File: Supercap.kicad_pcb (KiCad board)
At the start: 4 copper layers, 139 x 70.9 mm, 81 parts, among them IC1 NCP5109ADR2G, IC2 NCP5109ADR2G, J1 Conn_01x01, J2 Conn_01x01, J2-J1 Conn_01x10, J3 XT30, J3-J1 Conn_01x10, J4 XT30, P7803B-1000R1 P7803B-1000, P7812B-1000R1 490-P7812B-1000, U1 TLV2372, U2 TLV2372, U3 ACS71240KEXBLT-010B3, U4 LP-MSPM0G3507

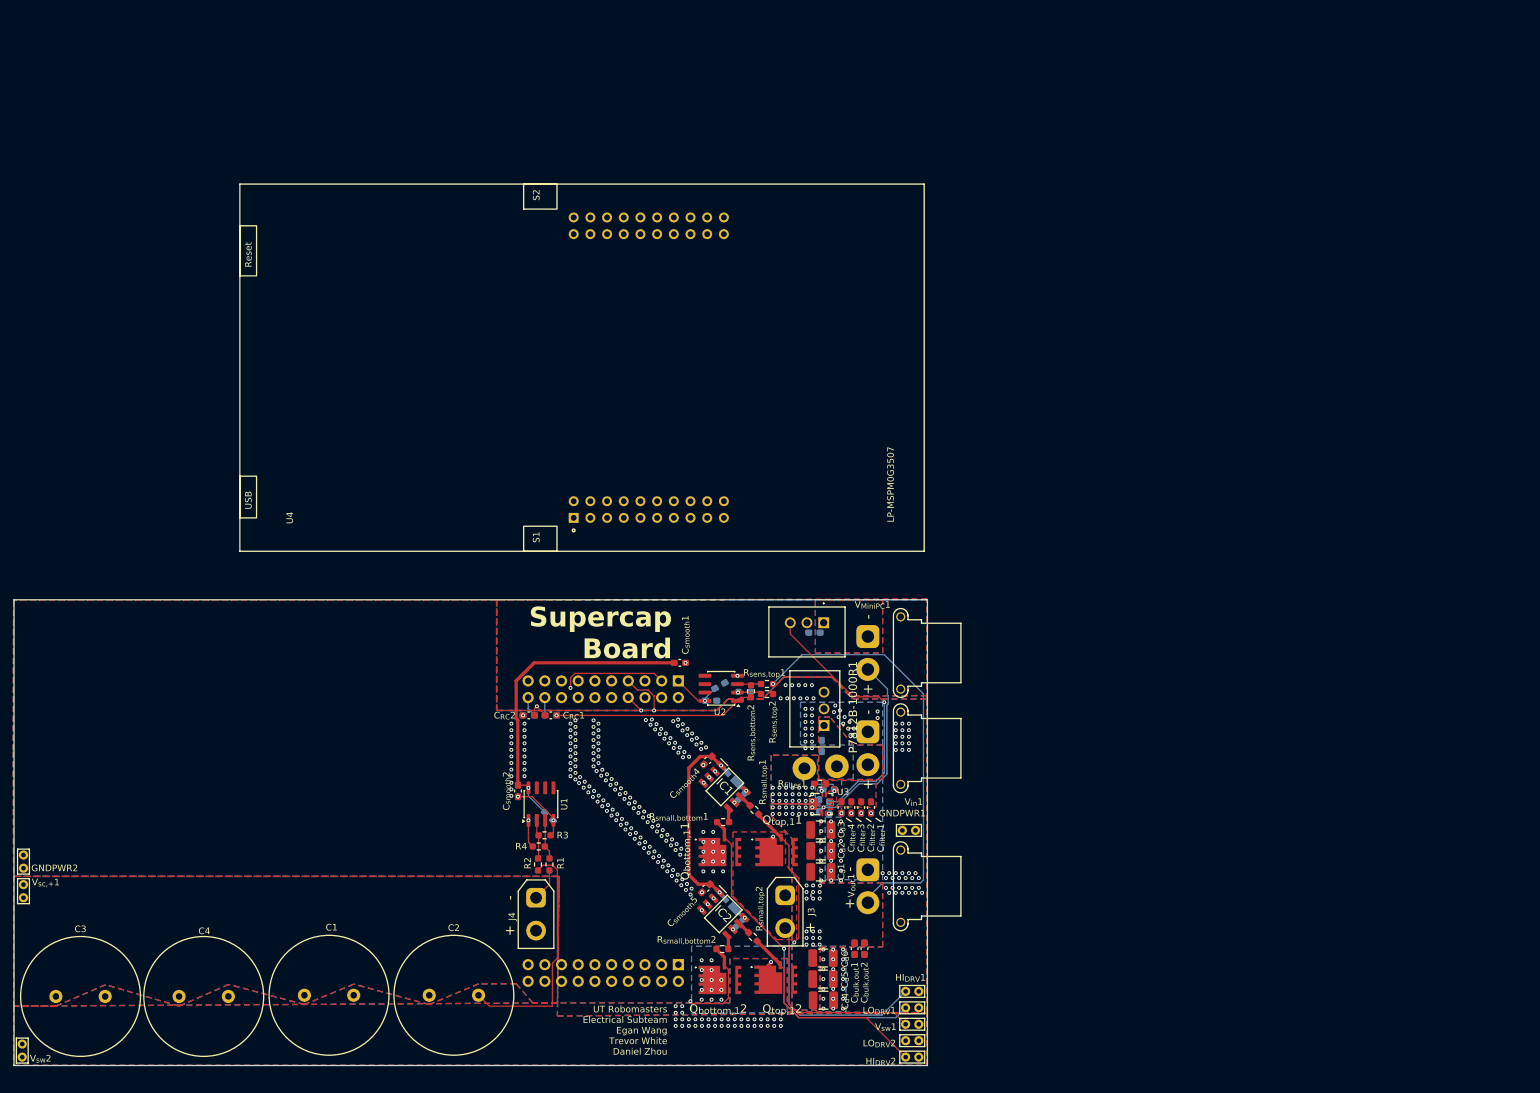
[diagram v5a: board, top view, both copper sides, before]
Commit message: split into separate boards as per regulations
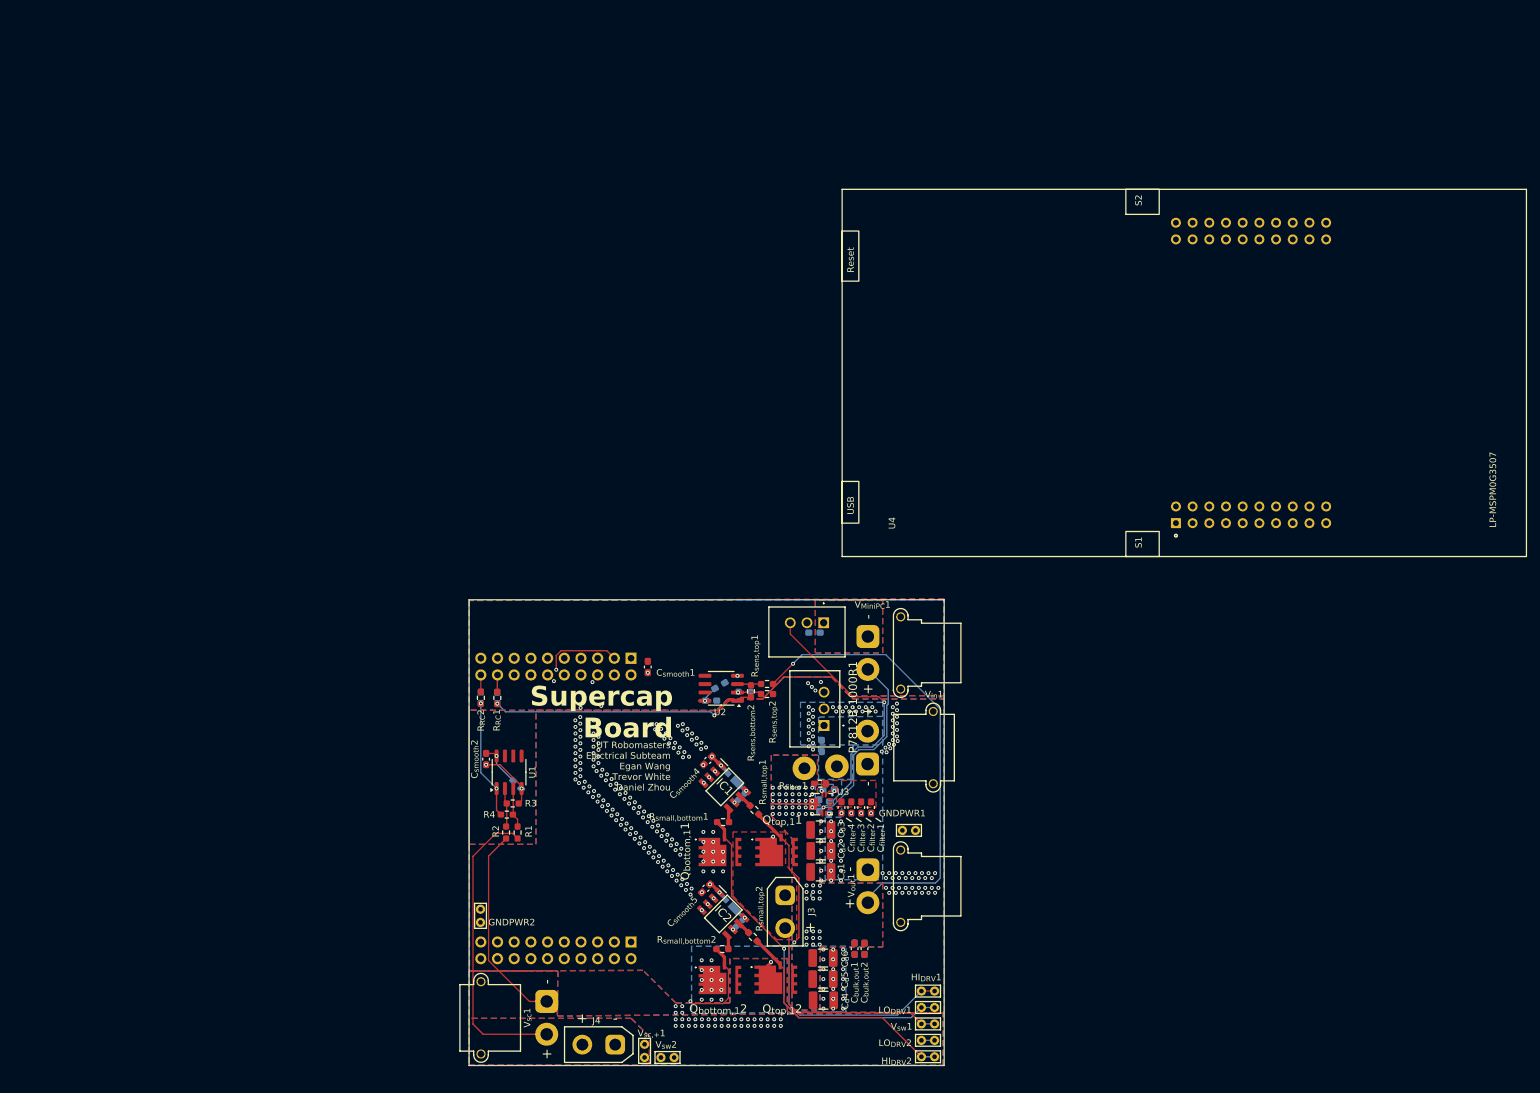
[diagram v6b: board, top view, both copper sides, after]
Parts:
- removed C1, C2, C3, C4: 110, Capacitor_THT:C_Radial_D18.0mm_H35.5mm_P7.50mm
- added V_{sc}1: Conn_01x02_Pin, Connector_AMASS:AMASS_XT30PW-M_1x02_P2.50mm_Horizontal, F.Cu at (103.6, 163.4)
- C_{RC}1, C_{RC}2: moved to B.Cu
- R_{RC}1, R_{RC}2: moved to F.Cu
- V_{in}1: footprint Connector_AMASS:AMASS_XT30PW-F_1x02_P2.50mm_Horizontal -> Connector_AMASS:AMASS_XT30PW-M_1x02_P2.50mm_Horizontal
- moved V_{sw}2 99.2 mm to (123.0, 171.9), turned to 180 degrees
- moved V_{sc,+}1 97.6 mm to (118.5, 171.9)
- moved U4 91.7 mm to (201.9, 67.7)
- moved GNDPWR2 70.0 mm to (93.6, 151.3)
- moved J4 25.4 mm to (114.1, 169.9), turned to 180 degrees
- moved C_{RC}1 8.56 mm to (96.1, 117.2), turned to 90 degrees
- moved R_{RC}1 8.56 mm to (96.1, 117.2), turned to 90 degrees
- moved J3-J1 7.98 mm to (116.5, 111.1)
- moved J2-J1 7.98 mm to (116.5, 154.3)
- moved C_{RC}2 7.77 mm to (93.6, 117.2), turned to 90 degrees
- moved R_{RC}2 7.77 mm to (93.6, 117.2), turned to 90 degrees
- moved R1 6.86 mm to (99.2, 137.7)
- moved R2 6.86 mm to (97.5, 137.7)
- moved C_{d}7 6.86 mm to (99.2, 130.4)
- moved C_{smooth}2 6.86 mm to (94.4, 126.5)
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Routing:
- net /Control/+3V3: track 97.4 -> 51.2 mm
- net /Control/V_{sc,+}: track 5.01 -> 46.0 mm
- net /Housekeeping/+12V: track 55.9 -> 94.5 mm, vias 2 -> 4
- net GND: track 61.9 -> 40.0 mm, vias 6 -> 9
- net /Control/PA22: track 18.1 -> 28.5 mm, vias 2 -> 1
- net /Control/PA8: track 20.2 -> 30.5 mm, vias 2 -> 1
- net /Control/V_{bat,sens}: track 30.7 -> 40.5 mm, vias 1 -> 2
- net /Control/PB9: track 41.6 -> 50.5 mm
- net /Control/F_bat: track 74.5 -> 82.5 mm
- net /Control/I_bat: track 66.8 -> 73.6 mm
- net /Voltage Converter/V_{sw,2}: track 48.1 -> 42.6 mm
- net /Control/I_{bat,out+}: track 65.9 -> 69.5 mm
- net /Control/V_{sc,sens}: track 21.1 -> 18.2 mm
- net /Voltage Converter/LO_DRV_{2}: track 52.8 -> 55.2 mm
- net /Voltage Converter/HI_DRV_{1}: track 54.0 -> 56.4 mm
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- removed copper zone on F.Cu, net /Control/I_{bat,in+}
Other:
- board size 139 x 70.9 mm -> 72.3 x 70.9 mm
- board text added: "MSMP0"

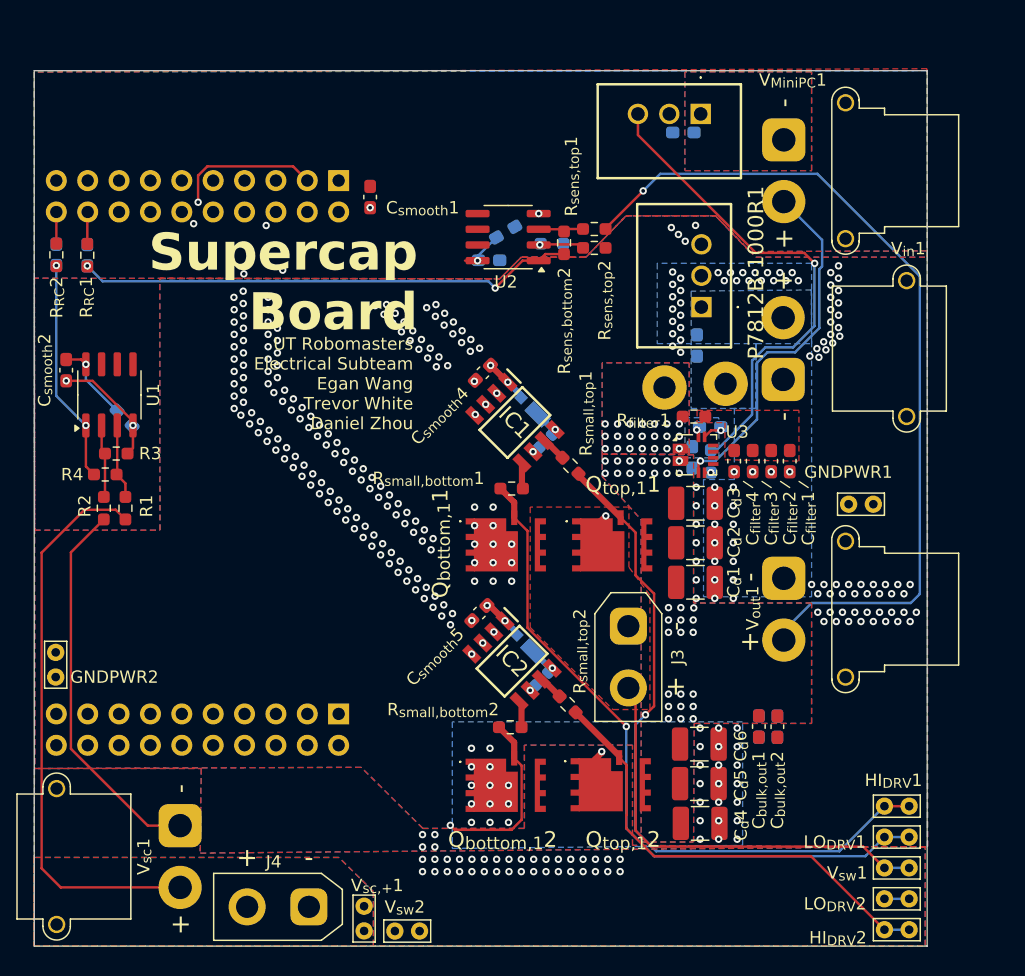
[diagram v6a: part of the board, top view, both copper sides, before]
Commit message: still need to finish housekeeping power supply footprints
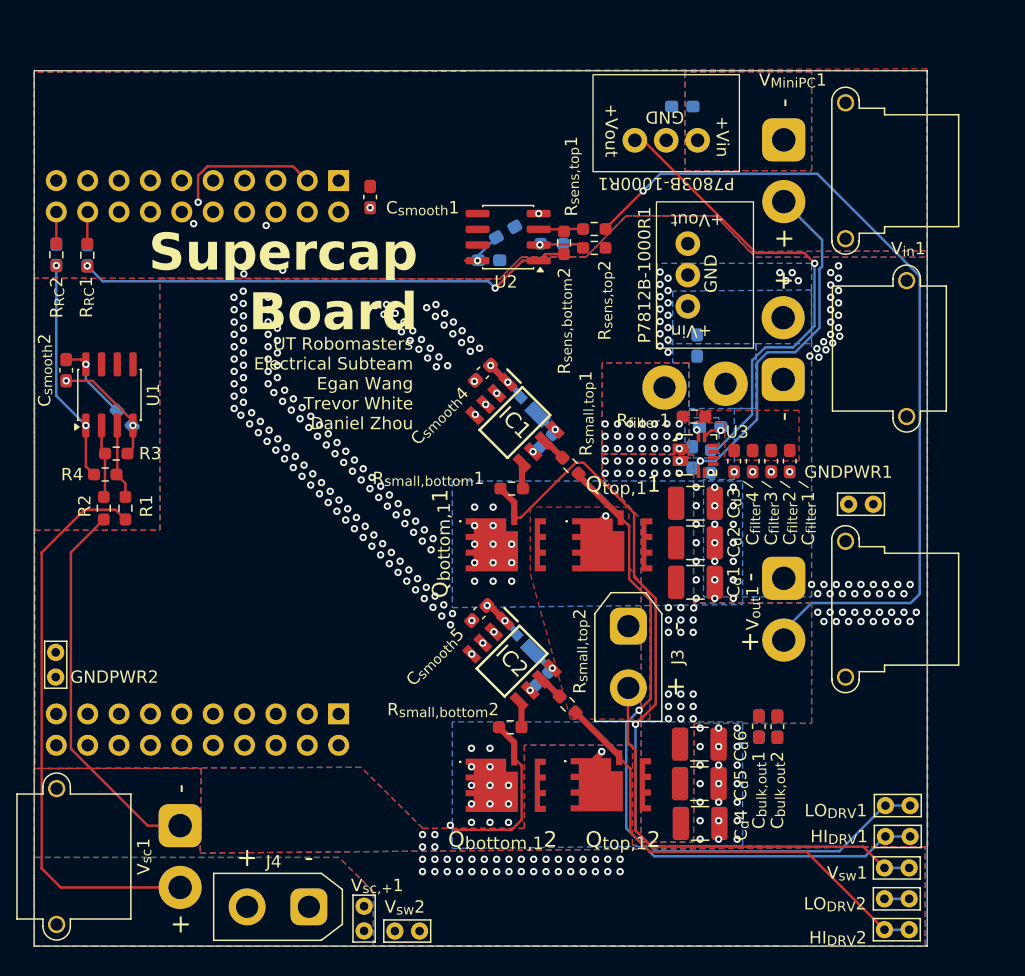
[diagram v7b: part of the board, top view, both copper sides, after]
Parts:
- P7803B-1000R1, P7812B-1000R1: footprint Robomaster_ICs:P7812B1000 -> Robomaster_ICs:P78B-1000R
- moved P7803B-1000R1 3.57 mm to (143.0, 107.9)
- moved P7812B-1000R1 2.87 mm to (144.7, 118.8)
- moved LO_{DRV}1 2.55 mm to (162.8, 161.8)
- moved HI_{DRV}1 2.45 mm to (162.8, 164.2)
- moved C_{smooth}6 2.10 mm to (144.3, 105.2)
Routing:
- net /Voltage Converter/LO_DRV_{1}: track 56.2 -> 67.5 mm
- net /Control/+3V3: track 51.2 -> 49.6 mm
- net /Housekeeping/+12V: track 94.5 -> 93.4 mm
- net GNDPWR: vias 310 -> 296

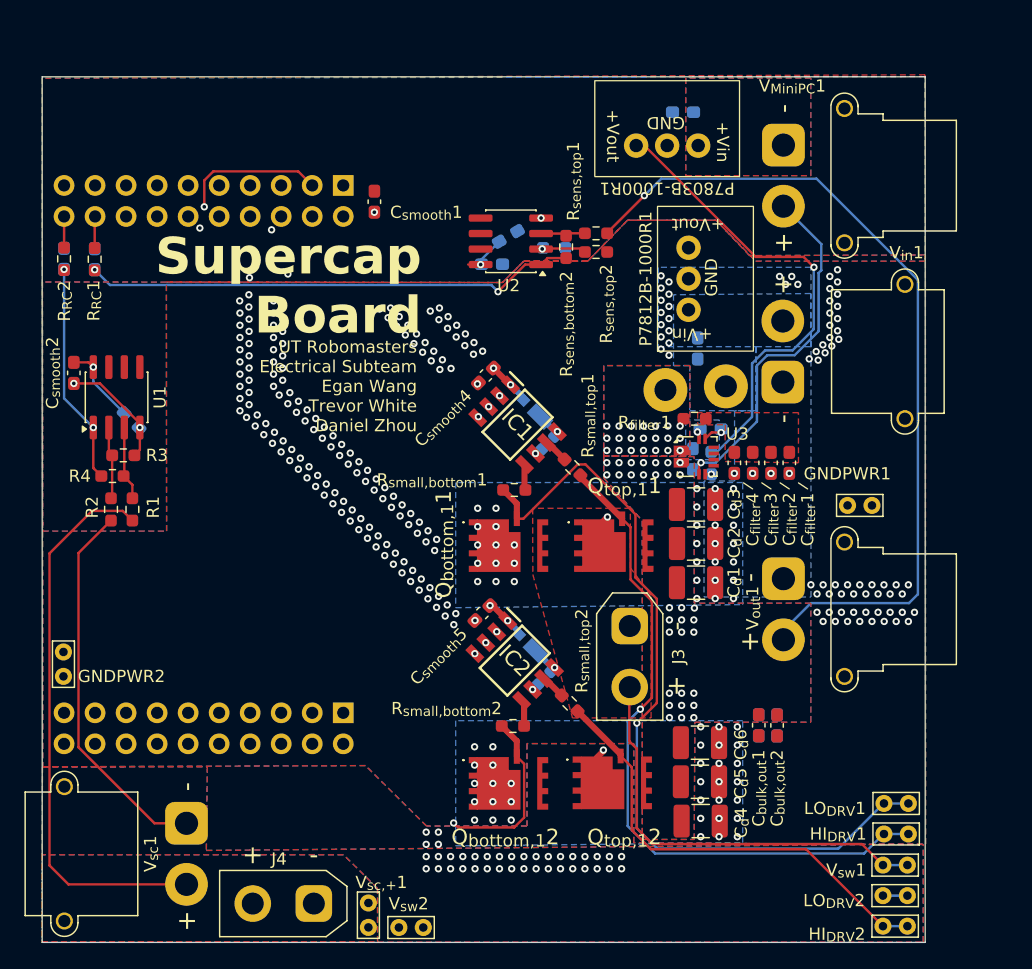
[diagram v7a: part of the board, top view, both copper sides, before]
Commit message: cleaned up PCB after meeting with BBJ
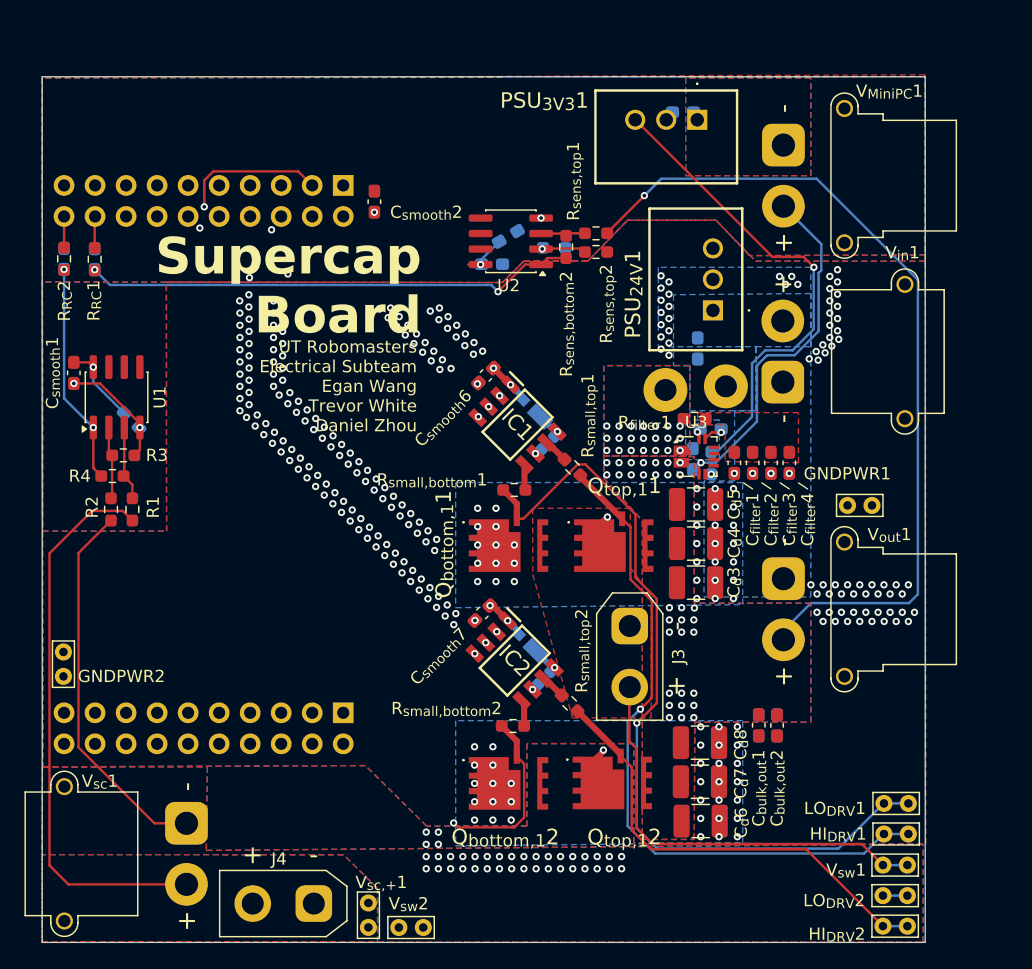
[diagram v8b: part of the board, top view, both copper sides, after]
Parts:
- PSU_{24V}1: renamed from P7812B-1000R1; footprint Robomaster_ICs:P78B-1000R -> Robomaster_ICs:P7812B1000
- PSU_{3V3}1: renamed from P7803B-1000R1; footprint Robomaster_ICs:P78B-1000R -> Robomaster_ICs:P7812B1000
- V_{MiniPC}1, V_{out}1: footprint Connector_AMASS:AMASS_XT30PW-F_1x02_P2.50mm_Horizontal -> Robomaster_Conn:AMASS_XT30PW-F_1x02_P2.50mm_Horizontal
- V_{in}1, V_{sc}1: footprint Connector_AMASS:AMASS_XT30PW-M_1x02_P2.50mm_Horizontal -> Robomaster_Conn:AMASS_XT30PW-M_1x02_P2.50mm_Horizontal
- moved PSU_{24V}1 3.33 mm to (146.8, 121.4)
- moved PSU_{3V3}1 3.30 mm to (145.5, 105.8)
- renumbered C_{d}7 to C_{d}1, C_{d}8 to C_{d}2, C_{d}1 to C_{d}3, C_{d}2 to C_{d}4, C_{d}3 to C_{d}5, C_{d}4 to C_{d}6, C_{d}5 to C_{d}7, C_{d}6 to C_{d}8, C_{filter}4 to C_{filter}1, C_{filter}3 to C_{filter}2, C_{filter}2 to C_{filter}3, C_{filter}1 to C_{filter}4, C_{smooth}2 to C_{smooth}1, C_{smooth}1 to C_{smooth}2, C_{smooth}6 to C_{smooth}4, C_{smooth}7 to C_{smooth}5, C_{smooth}4 to C_{smooth}6, C_{smooth}5 to C_{smooth}7
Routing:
- net /Housekeeping/+12V: track 93.4 -> 95.4 mm
- net /Control/+3V3: track 49.6 -> 50.5 mm
